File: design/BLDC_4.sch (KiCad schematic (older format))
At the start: 34 parts, among them K1 SERVO, P1 CANBUS, P10 MOTOR3, P11 MOTOR2, P12 MOTOR1, P14 IN+, P15 PWR_COMM, P2 HALL/Encoder, P3 HALL/Encoder, P4 PWR_COMM, P5 IN+, P6 IN-, P7 MOTOR3, P8 MOTOR2, P9 MOTOR1, X1 MINI-USB-SHIELD-32005-201

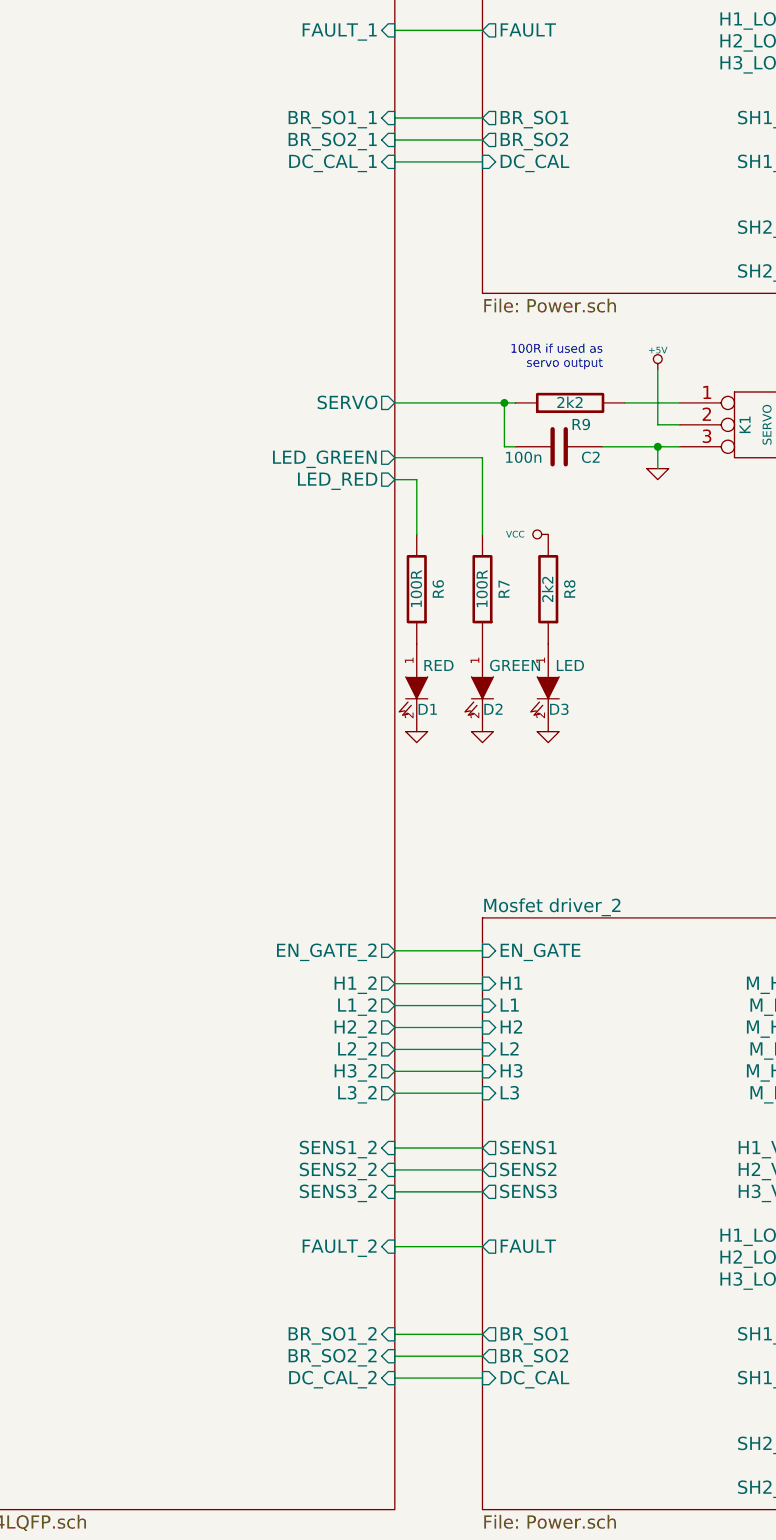
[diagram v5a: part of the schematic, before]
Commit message: Fix some ERC error, add decoupling cap to Vref+ and make some small changes to lib
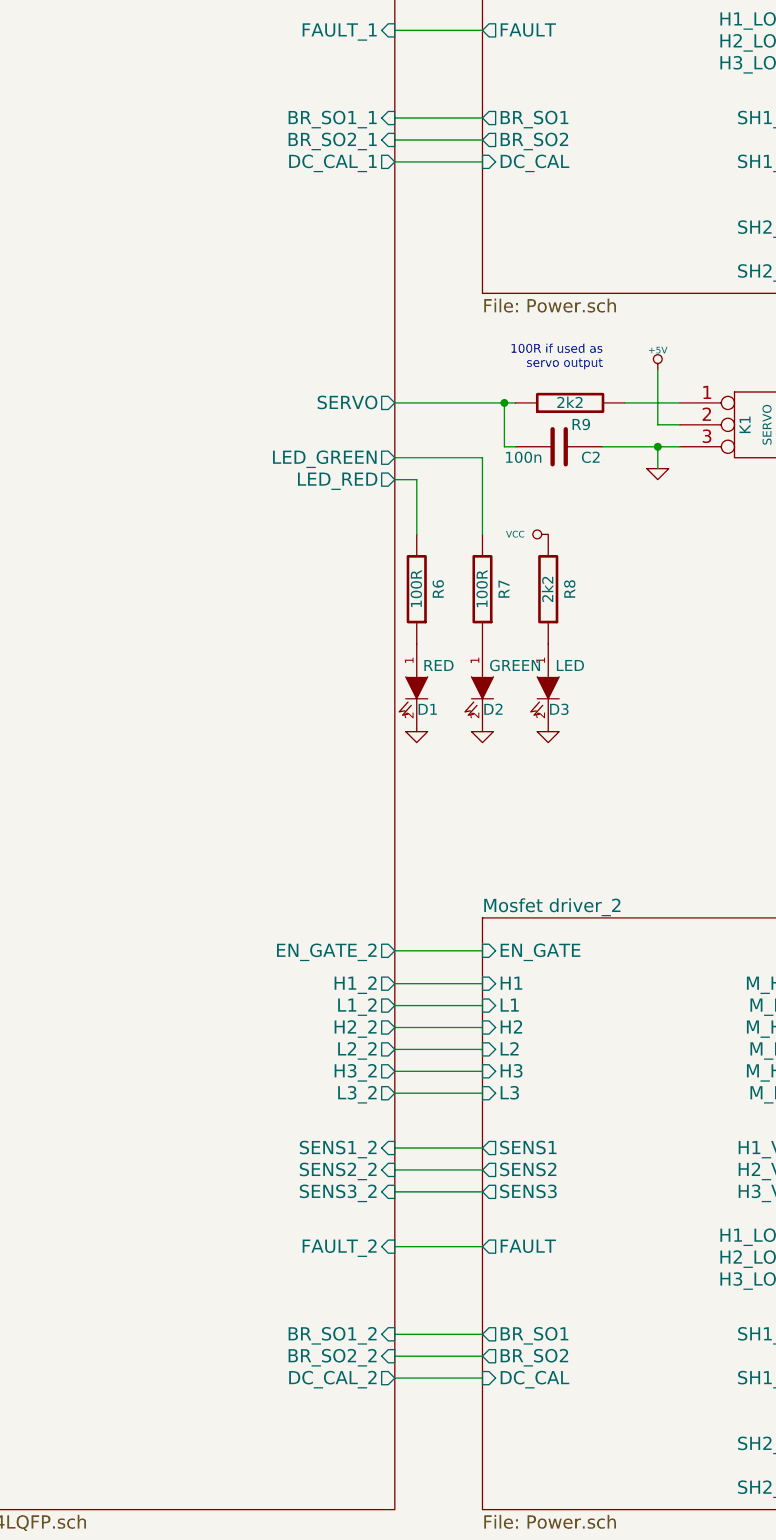
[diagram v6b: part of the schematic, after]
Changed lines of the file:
@@
 $EndComp
 $Comp
-L +5V #PWR3
+L +5V #PWR01
 U 1 1 522DA04D
 P 2850 5050
-F 0 "#PWR3" H 2850 5140 20  0001 C CNN
+F 0 "#PWR01" H 2850 5140 20  0001 C CNN
 F 1 "+5V" V 2800 5100 30  0000 C CNN
 F 2 "" H 2850 5050 60  0001 C CNN
@@
 $EndComp
 $Comp
-L GND #PWR7
+L GND #PWR02
 U 1 1 522DA053
 P 2900 4550
-F 0 "#PWR7" H 2900 4550 30  0001 C CNN
+F 0 "#PWR02" H 2900 4550 30  0001 C CNN
 F 1 "GND" H 2900 4480 30  0001 C CNN
 F 2 "" H 2900 4550 60  0001 C CNN
@@
 $EndComp
 $Comp
-L GND #PWR21
+L GND #PWR03
 U 1 1 522DA0BA
 P 8400 6000
-F 0 "#PWR21" H 8400 6000 30  0001 C CNN
+F 0 "#PWR03" H 8400 6000 30  0001 C CNN
 F 1 "GND" H 8400 5930 30  0001 C CNN
 F 2 "" H 8400 6000 60  0001 C CNN
@@
 V_SUPPLY
 $Comp
-L GND #PWR14
+L GND #PWR04
 U 1 1 522DA0CE
 P 3100 2650
-F 0 "#PWR14" H 3100 2650 30  0001 C CNN
+F 0 "#PWR04" H 3100 2650 30  0001 C CNN
 F 1 "GND" H 3100 2580 30  0001 C CNN
 F 2 "" H 3100 2650 60  0001 C CNN
@@
 $EndComp
 $Comp
-L GND #PWR5
+L GND #PWR05
 U 1 1 522DA0E2
 P 2850 6950
-F 0 "#PWR5" H 2850 6950 30  0001 C CNN
+F 0 "#PWR05" H 2850 6950 30  0001 C CNN
 F 1 "GND" H 2850 6880 30  0001 C CNN
 F 2 "" H 2850 6950 60  0001 C CNN
@@
 $EndComp
 $Comp
-L GND #PWR13
+L GND #PWR06
 U 1 1 522DA0FC
 P 3000 3600
-F 0 "#PWR13" H 3000 3600 30  0001 C CNN
+F 0 "#PWR06" H 3000 3600 30  0001 C CNN
 F 1 "GND" H 3000 3530 30  0001 C CNN
 F 2 "" H 3000 3600 60  0001 C CNN
@@
 $EndComp
 $Comp
-L +5V #PWR9
+L +5V #PWR07
 U 1 1 522DA11A
 P 2950 6750
-F 0 "#PWR9" H 2950 6840 20  0001 C CNN
+F 0 "#PWR07" H 2950 6840 20  0001 C CNN
 F 1 "+5V" V 2950 6900 30  0000 C CNN
 F 2 "" H 2950 6750 60  0001 C CNN
@@
 $EndComp
 $Comp
-L VCC #PWR10
+L VCC #PWR08
 U 1 1 522DA120
 P 2950 6850
-F 0 "#PWR10" H 2950 6950 30  0001 C CNN
+F 0 "#PWR08" H 2950 6950 30  0001 C CNN
 F 1 "VCC" V 2950 7000 30  0000 C CNN
 F 2 "" H 2950 6850 60  0001 C CNN
@@
 $EndComp
 $Comp
-L +5V #PWR20
+L +5V #PWR09
 U 1 1 522DA158
 P 8400 5550
-F 0 "#PWR20" H 8400 5640 20  0001 C CNN
+F 0 "#PWR09" H 8400 5640 20  0001 C CNN
 F 1 "+5V" H 8400 5640 30  0000 C CNN
 F 2 "" H 8400 5550 60  0001 C CNN
@@
 $EndComp
 $Comp
-L +5V #PWR15
+L +5V #PWR010
 U 1 1 522DA254
 P 4200 3050
-F 0 "#PWR15" H 4200 3140 20  0001 C CNN
+F 0 "#PWR010" H 4200 3140 20  0001 C CNN
 F 1 "+5V" H 4200 3140 30  0000 C CNN
 F 2 "" H 4200 3050 60  0001 C CNN
@@
 $EndComp
 $Comp
-L GND #PWR29
+L GND #PWR011
 U 1 1 53FA1F8F
 P 10850 6200
-F 0 "#PWR29" H 10850 6200 30  0001 C CNN
+F 0 "#PWR011" H 10850 6200 30  0001 C CNN
 F 1 "GND" H 10850 6130 30  0001 C CNN
 F 2 "" H 10850 6200 60  0001 C CNN
@@
 C8 C8 08 D2 A9 87 39 1B F9 3D 64 10 3C A5 22 3B 19 76 2F 98 2B 2B 2B 1E 8F A7 AB AB 0B FB AC 1D
 B9 73 C8 EF 2C EC 8D 33 57 03 96 70 05 29 43 0C 6A C5 A8 D7 30 9E 87 2D DE BE E8 EA 73 2F 9C 18
-F1 B3 C3 9F 6D FA 1E FF 03 71 17 46 7E 55 DF FF 4E 00 00 00 00 49 45 4E 44 AE 42 60 82 0C
+F1 B3 C3 9F 6D FA 1E FF 03 71 17 46 7E 55 DF FF 4E 00 00 00 00 49 45 4E 44 AE 42 60 82 0B
 EndData
 $EndBitmap
@@
 $EndSheet
 $Comp
-L GND #PWR2
+L GND #PWR012
 U 1 1 53FB6DA8
 P 2850 4200
-F 0 "#PWR2" H 2850 4200 30  0001 C CNN
+F 0 "#PWR012" H 2850 4200 30  0001 C CNN
 F 1 "GND" H 2850 4130 30  0001 C CNN
 F 2 "" H 2850 4200 60  0001 C CNN
@@
 $EndComp
 $Comp
-L GND #PWR16
+L GND #PWR013
 U 1 1 53FC021C
 P 7300 7200
-F 0 "#PWR16" H 7300 7200 30  0001 C CNN
+F 0 "#PWR013" H 7300 7200 30  0001 C CNN
 F 1 "GND" H 7300 7130 30  0001 C CNN
 F 2 "" H 7300 7200 60  0001 C CNN
@@
 $EndComp
 $Comp
-L GND #PWR17
+L GND #PWR014
 U 1 1 53FC131A
 P 7600 7200
-F 0 "#PWR17" H 7600 7200 30  0001 C CNN
+F 0 "#PWR014" H 7600 7200 30  0001 C CNN
 F 1 "GND" H 7600 7130 30  0001 C CNN
 F 2 "" H 7600 7200 60  0001 C CNN
@@
 $EndComp
 $Comp
-L GND #PWR19
+L GND #PWR015
 U 1 1 53FC8AA4
 P 7900 7200
-F 0 "#PWR19" H 7900 7200 30  0001 C CNN
+F 0 "#PWR015" H 7900 7200 30  0001 C CNN
 F 1 "GND" H 7900 7130 30  0001 C CNN
 F 2 "" H 7900 7200 60  0001 C CNN
@@
 $EndComp
 $Comp
-L VCC #PWR18
+L VCC #PWR016
 U 1 1 53FC98D2
 P 7900 6300
-F 0 "#PWR18" H 7900 6400 30  0001 C CNN
+F 0 "#PWR016" H 7900 6400 30  0001 C CNN
 F 1 "VCC" V 7900 6450 30  0000 C CNN
 F 2 "" H 7900 6300 60  0001 C CNN
@@
 $EndComp
 $Comp
-L +5V #PWR1
+L +5V #PWR017
 U 1 1 54036995
 P 2850 3900
-F 0 "#PWR1" H 2850 3990 20  0001 C CNN
+F 0 "#PWR017" H 2850 3990 20  0001 C CNN
 F 1 "+5V" H 2850 3990 30  0000 C CNN
 F 2 "" H 2850 3900 60  0001 C CNN
@@
 $EndComp
 $Comp
-L GND #PWR30
+L GND #PWR018
 U 1 1 548F24DF
 P 11150 6200
-F 0 "#PWR30" H 11150 6200 30  0001 C CNN
+F 0 "#PWR018" H 11150 6200 30  0001 C CNN
 F 1 "GND" H 11150 6130 30  0001 C CNN
 F 2 "" H 11150 6200 60  0001 C CNN
@@
 $EndComp
 $Comp
-L GND #PWR26
+L GND #PWR019
 U 1 1 548F2504
 P 9850 5250
-F 0 "#PWR26" H 9850 5250 30  0001 C CNN
+F 0 "#PWR019" H 9850 5250 30  0001 C CNN
 F 1 "GND" H 9850 5180 30  0001 C CNN
 F 2 "" H 9850 5250 60  0001 C CNN
@@
 $EndComp
 $Comp
-L GND #PWR22
+L GND #PWR020
 U 1 1 548F2529
 P 9550 4750
-F 0 "#PWR22" H 9550 4750 30  0001 C CNN
+F 0 "#PWR020" H 9550 4750 30  0001 C CNN
 F 1 "GND" H 9550 4680 30  0001 C CNN
 F 2 "" H 9550 4750 60  0001 C CNN
@@
 $EndComp
 $Comp
-L GND #PWR24
+L GND #PWR021
 U 1 1 548F254E
 P 9700 4250
-F 0 "#PWR24" H 9700 4250 30  0001 C CNN
+F 0 "#PWR021" H 9700 4250 30  0001 C CNN
 F 1 "GND" H 9700 4180 30  0001 C CNN
 F 2 "" H 9700 4250 60  0001 C CNN
@@
 $EndComp
 $Comp
-L GND #PWR28
+L GND #PWR022
 U 1 1 548F2573
 P 10500 1650
-F 0 "#PWR28" H 10500 1650 30  0001 C CNN
+F 0 "#PWR022" H 10500 1650 30  0001 C CNN
 F 1 "GND" H 10500 1580 30  0001 C CNN
 F 2 "" H 10500 1650 60  0001 C CNN
@@
 $EndComp
 $Comp
-L +5V #PWR4
+L +5V #PWR023
 U 1 1 54B6A9FD
 P 2850 6100
-F 0 "#PWR4" H 2850 6190 20  0001 C CNN
+F 0 "#PWR023" H 2850 6190 20  0001 C CNN
 F 1 "+5V" V 2800 6150 30  0000 C CNN
 F 2 "" H 2850 6100 60  0001 C CNN
@@
 $EndComp
 $Comp
-L GND #PWR8
+L GND #PWR024
 U 1 1 54B6AA03
 P 2900 5600
-F 0 "#PWR8" H 2900 5600 30  0001 C CNN
+F 0 "#PWR024" H 2900 5600 30  0001 C CNN
 F 1 "GND" H 2900 5530 30  0001 C CNN
 F 2 "" H 2900 5600 60  0001 C CNN
@@
 C8 C8 08 D2 A9 87 39 1B F9 3D 64 10 3C A5 22 3B 19 76 2F 98 2B 2B 2B 1E 8F A7 AB AB 0B FB AC 1D
 B9 73 C8 EF 2C EC 8D 33 57 03 96 70 05 29 43 0C 6A C5 A8 D7 30 9E 87 2D DE BE E8 EA 73 2F 9C 18
-F1 B3 C3 9F 6D FA 1E FF 03 71 17 46 7E 55 DF FF 4E 00 00 00 00 49 45 4E 44 AE 42 60 82 0C
+F1 B3 C3 9F 6D FA 1E FF 03 71 17 46 7E 55 DF FF 4E 00 00 00 00 49 45 4E 44 AE 42 60 82 0B
 EndData
 $EndBitmap
@@
 $EndComp
 $Comp
-L GND #PWR27
+L GND #PWR025
 U 1 1 54B73612
 P 9850 10800
-F 0 "#PWR27" H 9850 10800 30  0001 C CNN
+F 0 "#PWR025" H 9850 10800 30  0001 C CNN
 F 1 "GND" H 9850 10730 30  0001 C CNN
 F 2 "" H 9850 10800 60  0001 C CNN
@@
 $EndComp
 $Comp
-L GND #PWR23
+L GND #PWR026
 U 1 1 54B73618
 P 9550 10300
-F 0 "#PWR23" H 9550 10300 30  0001 C CNN
+F 0 "#PWR026" H 9550 10300 30  0001 C CNN
 F 1 "GND" H 9550 10230 30  0001 C CNN
 F 2 "" H 9550 10300 60  0001 C CNN
@@
 $EndComp
 $Comp
-L GND #PWR25
+L GND #PWR027
 U 1 1 54B7361E
 P 9700 9800
-F 0 "#PWR25" H 9700 9800 30  0001 C CNN
+F 0 "#PWR027" H 9700 9800 30  0001 C CNN
 F 1 "GND" H 9700 9730 30  0001 C CNN
 F 2 "" H 9700 9800 60  0001 C CNN
@@
 	10050 2050 10050 1200
 $Comp
-L GND #PWR6
+L GND #PWR028
 U 1 1 54DE4953
 P 2850 7850
-F 0 "#PWR6" H 2850 7850 30  0001 C CNN
+F 0 "#PWR028" H 2850 7850 30  0001 C CNN
 F 1 "GND" H 2850 7780 30  0001 C CNN
 F 2 "" H 2850 7850 60  0001 C CNN
@@
 $EndComp
 $Comp
-L +5V #PWR11
+L +5V #PWR029
 U 1 1 54DE495F
 P 2950 7650
-F 0 "#PWR11" H 2950 7740 20  0001 C CNN
+F 0 "#PWR029" H 2950 7740 20  0001 C CNN
 F 1 "+5V" V 2950 7800 30  0000 C CNN
 F 2 "" H 2950 7650 60  0001 C CNN
@@
 $EndComp
 $Comp
-L VCC #PWR12
+L VCC #PWR030
 U 1 1 54DE4965
 P 2950 7750
-F 0 "#PWR12" H 2950 7850 30  0001 C CNN
+F 0 "#PWR030" H 2950 7850 30  0001 C CNN
 F 1 "VCC" V 2950 7900 30  0000 C CNN
 F 2 "" H 2950 7750 60  0001 C CNN
@@
 F35 "BR_SO1_1" I R 7200 4400 60
 F36 "BR_SO2_1" I R 7200 4500 60
-F37 "DC_CAL_1" I R 7200 4600 60
-F38 "DC_CAL_2" I R 7200 10150 60
-F39 "FAULT_2" I R 7200 9550 60
-F40 "EN_GATE_2" O R 7200 8200 60
-F41 "L3_2" O R 7200 8850 60
-F42 "L2_2" O R 7200 8650 60
-F43 "L1_2" O R 7200 8450 60
-F44 "H3_2" O R 7200 8750 60
-F45 "H2_2" O R 7200 8550 60
-F46 "H1_2" O R 7200 8350 60
-F47 "RX_SCL_1" O L 4650 7250 60
-F48 "TX_SDA_1" T L 4650 7150 60
-F49 "ADC_EXT_1" I L 4650 7050 60
-F50 "TX_SDA_2" T L 4650 8050 60
-F51 "RX_SCL_2" O L 4650 8150 60
-F52 "ADC_EXT_2" I L 4650 7950 60
+F37 "FAULT_2" I R 7200 9550 60
+F38 "EN_GATE_2" O R 7200 8200 60
+F39 "L3_2" O R 7200 8850 60
+F40 "L2_2" O R 7200 8650 60
+F41 "L1_2" O R 7200 8450 60
+F42 "H3_2" O R 7200 8750 60
+F43 "H2_2" O R 7200 8550 60
+F44 "H1_2" O R 7200 8350 60
+F45 "RX_SCL_1" O L 4650 7250 60
+F46 "TX_SDA_1" T L 4650 7150 60
+F47 "ADC_EXT_1" I L 4650 7050 60
+F48 "TX_SDA_2" T L 4650 8050 60
+F49 "RX_SCL_2" O L 4650 8150 60
+F50 "ADC_EXT_2" I L 4650 7950 60
+F51 "DC_CAL_1" O R 7200 4600 60
+F52 "DC_CAL_2" O R 7200 10150 60
 $EndSheet
 $EndSCHEMATC

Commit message: Some fixes in libs,schemas and netlist. Start new PCB
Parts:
- P1: footprint CRF1:pinhead-1X03 -> CRF1:pinhead-1X04
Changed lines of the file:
@@
 C8 C8 08 D2 A9 87 39 1B F9 3D 64 10 3C A5 22 3B 19 76 2F 98 2B 2B 2B 1E 8F A7 AB AB 0B FB AC 1D
 B9 73 C8 EF 2C EC 8D 33 57 03 96 70 05 29 43 0C 6A C5 A8 D7 30 9E 87 2D DE BE E8 EA 73 2F 9C 18
-F1 B3 C3 9F 6D FA 1E FF 03 71 17 46 7E 55 DF FF 4E 00 00 00 00 49 45 4E 44 AE 42 60 82 0B
+F1 B3 C3 9F 6D FA 1E FF 03 71 17 46 7E 55 DF FF 4E 00 00 00 00 49 45 4E 44 AE 42 60 82 03
 EndData
 $EndBitmap
@@
 F 0 "P1" H 2500 3800 50  0000 C CNN
 F 1 "CANBUS" H 2500 4300 40  0000 C CNN
-F 2 "CRF1:pinhead-1X03" H 2500 4100 60  0001 C CNN
+F 2 "CRF1:pinhead-1X04" H 2500 4100 60  0001 C CNN
 F 3 "" H 2500 4100 60  0000 C CNN
 	1    2500 4050
@@
 C8 C8 08 D2 A9 87 39 1B F9 3D 64 10 3C A5 22 3B 19 76 2F 98 2B 2B 2B 1E 8F A7 AB AB 0B FB AC 1D
 B9 73 C8 EF 2C EC 8D 33 57 03 96 70 05 29 43 0C 6A C5 A8 D7 30 9E 87 2D DE BE E8 EA 73 2F 9C 18
-F1 B3 C3 9F 6D FA 1E FF 03 71 17 46 7E 55 DF FF 4E 00 00 00 00 49 45 4E 44 AE 42 60 82 0B
+F1 B3 C3 9F 6D FA 1E FF 03 71 17 46 7E 55 DF FF 4E 00 00 00 00 49 45 4E 44 AE 42 60 82 03
 EndData
 $EndBitmap

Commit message: Start work on pcb
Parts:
- P15: value PWR_COMM -> PWR_COMM_2
- P4: value PWR_COMM -> PWR_COMM_1
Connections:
- net ADC_EXT renamed ADC_EXT_1
- net ADC_EXT_1: no longer P15.3
- net RX_SCL renamed RX_SCL_1
- net RX_SCL_1: no longer P15.1
- net TX_SDA renamed TX_SDA_1
- net TX_SDA_1: no longer P15.2
- new net ADC_EXT_2: P15.3
- new net RX_SCL_2: P15.1
- new net TX_SDA_2: P15.2
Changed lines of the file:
@@
 P 2500 7000
 F 0 "P4" H 2500 6650 60  0000 C CNN
-F 1 "PWR_COMM" H 2500 7350 60  0000 C CNN
+F 1 "PWR_COMM_1" H 2500 7350 60  0000 C CNN
 F 2 "CRF1:MICRO_JST_6" H 2500 7000 60  0001 C CNN
 F 3 "" H 2500 7000 60  0001 C CNN
@@
 V_SUPPLY
 Text Label 2850 7250 0    40   ~ 0
-RX_SCL
+RX_SCL_1
 Text Label 2850 7150 0    40   ~ 0
-TX_SDA
+TX_SDA_1
 Text Label 2850 7050 0    40   ~ 0
-ADC_EXT
+ADC_EXT_1
 Text Notes 2550 1400 0    340  ~ 68
 BLDC motor controller
@@
 C8 C8 08 D2 A9 87 39 1B F9 3D 64 10 3C A5 22 3B 19 76 2F 98 2B 2B 2B 1E 8F A7 AB AB 0B FB AC 1D
 B9 73 C8 EF 2C EC 8D 33 57 03 96 70 05 29 43 0C 6A C5 A8 D7 30 9E 87 2D DE BE E8 EA 73 2F 9C 18
-F1 B3 C3 9F 6D FA 1E FF 03 71 17 46 7E 55 DF FF 4E 00 00 00 00 49 45 4E 44 AE 42 60 82 03
+F1 B3 C3 9F 6D FA 1E FF 03 71 17 46 7E 55 DF FF 4E 00 00 00 00 49 45 4E 44 AE 42 60 82 01
 EndData
 $EndBitmap
@@
 C8 C8 08 D2 A9 87 39 1B F9 3D 64 10 3C A5 22 3B 19 76 2F 98 2B 2B 2B 1E 8F A7 AB AB 0B FB AC 1D
 B9 73 C8 EF 2C EC 8D 33 57 03 96 70 05 29 43 0C 6A C5 A8 D7 30 9E 87 2D DE BE E8 EA 73 2F 9C 18
-F1 B3 C3 9F 6D FA 1E FF 03 71 17 46 7E 55 DF FF 4E 00 00 00 00 49 45 4E 44 AE 42 60 82 03
+F1 B3 C3 9F 6D FA 1E FF 03 71 17 46 7E 55 DF FF 4E 00 00 00 00 49 45 4E 44 AE 42 60 82 01
 EndData
 $EndBitmap
@@
 P 2500 7900
 F 0 "P15" H 2500 7550 60  0000 C CNN
-F 1 "PWR_COMM" H 2500 8250 60  0000 C CNN
+F 1 "PWR_COMM_2" H 2500 8250 60  0000 C CNN
 F 2 "CRF1:MICRO_JST_6" H 2500 7900 60  0001 C CNN
 F 3 "" H 2500 7900 60  0001 C CNN
@@
 $EndComp
 Text Label 2850 8150 0    40   ~ 0
-RX_SCL
+RX_SCL_2
 Text Label 2850 8050 0    40   ~ 0
-TX_SDA
+TX_SDA_2
 Text Label 2850 7950 0    40   ~ 0
-ADC_EXT
+ADC_EXT_2
 Wire Wire Line
 	2950 7650 2850 7650
@@
 F52 "DC_CAL_2" O R 7200 10150 60
 $EndSheet
+Entry Bus Bus
+	6900 7300 7000 7400
 $EndSCHEMATC
